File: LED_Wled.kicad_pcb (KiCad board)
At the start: 2 copper layers, 100 x 97.5 mm, 131 parts, among them J1 SWD_PORT_SKEDD, J2 Screw_Terminal_01x02, J3 Screw_Terminal_01x03, Q1 BSS138, U1 ESP8266-12E_ESP-12E, U2 AMS1117-3.3, U3 AMS1117-5.0

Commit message: updated to rev1.1
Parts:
- removed the C1 at (142.0, 128.8)
- removed the C1 at (78.0, 139.2)
- removed the C1 at (142.0, 100.8)
- removed the C1 at (78.0, 111.2)
- removed the C1 at (142.0, 72.8)
- removed the C1 at (78.0, 83.2)
- removed the C2 at (142.0, 123.2)
- removed the C2 at (78.0, 144.8)
- removed the C2 at (142.0, 95.2)
- removed the C2 at (78.0, 116.8)
- removed the C2 at (142.0, 67.2)
- removed the C2 at (78.0, 88.8)
- removed the C3 at (140.0, 131.7)
- removed the C3 at (80.0, 136.3)
- removed the C3 at (140.0, 103.7)
- removed the C3 at (80.0, 108.3)
- removed the C3 at (140.0, 75.7)
- removed the C3 at (80.0, 80.3)
- removed the C4 at (141.3, 134.6)
- removed the C4 at (78.7, 133.4)
- removed the C4 at (141.3, 106.5)
- removed the C4 at (78.7, 105.5)
- removed the C4 at (141.3, 78.5)
- removed the C4 at (78.7, 77.5)
- removed the D1 at (136.3, 134.0)
- removed the D1 at (83.7, 134.0)
- removed the D1 at (136.3, 106.0)
- removed the D1 at (83.7, 106.0)
- removed the D1 at (136.3, 78.0)
- removed the D1 at (83.7, 78.0)
- removed G*** (x6): LOGO, LED_Wled:es
- removed the J1 at (136.2, 143.7)
- removed the J1 at (83.8, 124.3)
- removed the J1 at (136.2, 115.7)
- removed the J1 at (83.8, 96.3)
- removed the J1 at (136.2, 87.7)
- removed the J1 at (83.8, 68.3)
- removed the J2 at (147.0, 144.8)
- removed the J2 at (73.0, 123.2)
- removed the J2 at (147.0, 116.8)
- removed the J2 at (73.0, 95.2)
- removed the J2 at (147.0, 88.8)
- removed the J2 at (73.0, 67.2)
- removed the J3 at (147.0, 137.8)
- removed the J3 at (73.0, 130.2)
- removed the J3 at (147.0, 109.8)
- removed the J3 at (73.0, 102.2)
- removed the J3 at (147.0, 81.8)
- removed the J3 at (73.0, 74.2)
- removed JP1 (x6): Jumper, Jumper:SolderJumper-2_P1.3mm_Open_RoundedPad1.0x1.5mm
- removed the Q1 at (140.0, 138.3)
- removed the Q1 at (80.0, 129.7)
- removed the Q1 at (140.0, 110.3)
- removed the Q1 at (80.0, 101.7)
- removed the Q1 at (140.0, 82.3)
- removed the Q1 at (80.0, 73.7)
- removed the R1 at (132.7, 134.3)
- removed the R1 at (87.3, 133.7)
- removed the R1 at (132.7, 106.3)
- removed the R1 at (87.3, 105.7)
- removed the R1 at (132.7, 78.3)
- removed the R1 at (87.3, 77.7)
- removed the R2 at (132.7, 138.2)
- removed the R2 at (87.3, 129.8)
- removed the R2 at (132.7, 110.2)
- removed the R2 at (87.3, 101.8)
- removed the R2 at (132.7, 82.2)
- removed the R2 at (87.3, 73.8)
- removed the R3 at (132.0, 128.8)
- removed the R3 at (88.0, 139.2)
- removed the R3 at (132.0, 100.8)
- removed the R3 at (88.0, 111.2)
- removed the R3 at (132.0, 72.8)
- removed the R3 at (88.0, 83.2)
- removed the R4 at (136.3, 138.6)
- removed the R4 at (83.7, 129.4)
- removed the R4 at (136.3, 110.6)
- removed the R4 at (83.7, 101.4)
- removed the R4 at (136.3, 82.6)
- removed the R4 at (83.7, 73.4)
- removed the R5 at (139.2, 134.5)
- removed the R5 at (80.8, 133.5)
- removed the R5 at (139.2, 106.5)
- removed the R5 at (80.8, 105.5)
- removed the R5 at (139.2, 78.5)
- removed the R5 at (80.8, 77.5)
- removed the U1 at (120.5, 131.0)
- removed the U1 at (99.5, 137.0)
- removed the U1 at (120.5, 103.0)
- removed the U1 at (99.5, 109.0)
- removed the U1 at (120.5, 75.0)
- removed the U1 at (99.5, 81.0)
- removed the U2 at (136.8, 126.0)
- removed the U2 at (83.2, 142.0)
- removed the U2 at (136.8, 98.0)
- removed the U2 at (83.2, 114.0)
- removed the U2 at (136.8, 70.0)
- removed the U2 at (83.2, 86.0)
- removed the U3 at (147.4, 126.0)
- removed the U3 at (72.6, 142.0)
- removed the U3 at (147.4, 98.0)
- removed the U3 at (72.6, 114.0)
- removed the U3 at (147.4, 70.0)
- removed the U3 at (72.6, 86.0)
- removed mouse-bite-2mm-slot (x17): VAL**, Panelization:mouse-bite-2mm-slot
- added BOOT1: Jumper, Connector_PinHeader_1.27mm:PinHeader_1x02_P1.27mm_Vertical, F.Cu at (112.9, 71.2)
- added C1: 180uF/35V, Capacitor_SMD:CP_Elec_10x12.5, F.Cu at (97.0, 66.8)
- added C2: 470uF/35V, Capacitor_SMD:C_Elec_10x10.2, F.Cu at (84.3, 52.2)
- added C3: 1uF/50V, Capacitor_SMD:C_1206_3216Metric, F.Cu at (93.0, 51.2)
- added C4: 100nF/50V, Capacitor_SMD:C_0805_2012Metric, F.Cu at (110.7, 59.9)
- added C5: 10uF/50V, Capacitor_SMD:C_1206_3216Metric, F.Cu at (112.3, 63.5)
- added D1: SS32, Diode_SMD:D_SMC, F.Cu at (95.3, 57.5)
- added J1: SWD_PORT_SKEDD, LED_Wled:WR_WST_REDFIT_IDC_4Pin, F.Cu at (101.5, 50.0)
- added J2: Screw_Terminal_01x02, TerminalBlock_MetzConnect:TerminalBlock_MetzConnect_Type086_RT03402HBLC_1x02_P3.81mm_Horizontal, F.Cu at (71.8, 53.0)
- added J3: Screw_Terminal_01x03, TerminalBlock_MetzConnect:TerminalBlock_MetzConnect_Type086_RT03403HBLC_1x03_P3.81mm_Horizontal, F.Cu at (71.8, 70.0)
- added L1: 68uH, Inductor_SMD:L_12x12mm_H8mm, F.Cu at (83.0, 65.7)
- added NT1: Net-Tie_2, NetTie:NetTie-2_SMD_Pad2.0mm, F.Cu at (75.5, 57.7)
- added Q1: BSS138, Package_TO_SOT_SMD:SOT-23, F.Cu at (110.7, 50.9)
- added R1: 10k, Resistor_SMD:R_0805_2012Metric, F.Cu at (110.7, 55.8)
- added R2: 10k, Resistor_SMD:R_0805_2012Metric, F.Cu at (110.7, 53.8)
- added R3: 10k, Resistor_SMD:R_0805_2012Metric, F.Cu at (110.7, 57.9)
- added R4: 10k, Resistor_SMD:R_0805_2012Metric, F.Cu at (113.6, 50.9)
- added R5: 10k, Resistor_SMD:R_0805_2012Metric, F.Cu at (110.7, 48.1)
- added U1: ESP8266-12E_ESP-12E, LED_Wled:ESP-12E, F.Cu at (123.5, 62.5)
- added U2: XL1509, Package_SO:SOP-8_3.9x4.9mm_P1.27mm, F.Cu at (104.6, 57.6)
- added U3: LD1117DT33TR, Package_TO_SOT_SMD:TO-252-2, F.Cu at (107.5, 66.8)
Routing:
- net (no net): track 1340.2 -> 0.00 mm, vias 115 -> 0
- net LED_OUT_HV: track 11.2 -> 101.3 mm, vias 0 -> 1
- net VIN: track 25.1 -> 69.9 mm, vias 1 -> 0
- net Net-(D1-Pad1): track 0.00 -> 38.7 mm, vias 0 -> 2
- net Net-(BOOT1-Pad2): track 0.00 -> 30.8 mm
- net +5V: track 18.1 -> 47.0 mm
- net Net-(JP1-Pad2): track 21.1 -> 0.00 mm, vias 2 -> 0
- net /PROT_VIN: track 18.5 -> 0.00 mm
- net GNDPWR: track 0.00 -> 10.8 mm
- net TXD: track 26.8 -> 35.6 mm, vias 0 -> 1
- net Net-(R3-Pad1): track 20.3 -> 28.3 mm
- net RXD: track 25.9 -> 31.4 mm, vias 0 -> 1
- net Net-(R1-Pad2): track 3.91 -> 7.27 mm
- net LED_OUT_LV: track 39.8 -> 37.7 mm, vias 3 -> 0
- net GND: track 9.71 -> 7.65 mm, vias 13 -> 57
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- removed copper zone on B.Cu, net (none)
- removed copper zone on F.Cu, net (none)
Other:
- board size 100 x 97.5 mm -> 66 x 27 mm
- board text added: "For use with ARGB LED-strip MAX INPUT: +30 V"
- board text added: "remote-led-project 2022-01-13 rev1.1"
- board text removed: "+3v3"
- board text removed: "DI VIN GND"
- board text removed: "For use with ARGB LED-strip MAX INPUT: +13V"
- board text removed: "GND"
- board text removed: "RX"
- board text removed: "TX"
- board text removed: "VIN GND"
- board text removed: "remote-led-project 2021-11-04 rev1.0"

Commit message: Update LED_Wled.kicad_pcb
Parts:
- added G***: LOGO, LED_Wled:es, B.Cu at (122.2, 60.0)

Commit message: finished rev1.1
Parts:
- removed G***: LOGO, LED_Wled:es
- added F1: Fuse_Small, Fuse:Fuse_1812_4532Metric, F.Cu at (93.3, 50.6)
- C1: value 180uF/35V -> 180uF/63V; footprint Capacitor_SMD:CP_Elec_10x12.5 -> Capacitor_THT:C_Radial_D10.0mm_H16.0mm_P5.00mm
- J2: value Screw_Terminal_01x02 -> KF141V-2.54-2P; footprint TerminalBlock_MetzConnect:TerminalBlock_MetzConnect_Type086_RT03402HBLC_1x02_P3.81mm_Horizontal -> userdvc:KF141V-2.54-2P
- J3: value Screw_Terminal_01x03 -> KF141V-2.54-3P; footprint TerminalBlock_MetzConnect:TerminalBlock_MetzConnect_Type086_RT03403HBLC_1x03_P3.81mm_Horizontal -> userdvc:KF141V-2.54-3P
- moved C3 10.0 mm to (85.9, 58.3), turned to 180 degrees
- moved J3 4.39 mm to (70.0, 66.0), turned to 270 degrees
- moved C1 3.76 mm to (100.8, 66.5)
- moved J2 2.34 mm to (70.0, 51.5), turned to 270 degrees
- moved L1 0.78 mm to (83.5, 66.3)
- moved NT1 0.74 mm to (76.0, 58.2)
- moved C2 0.71 mm to (84.2, 51.5)
- moved J1 0.50 mm to (102.0, 50.0)
- moved D1 0.20 mm to (95.5, 57.5)
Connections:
- C2 pad 1: VIN -> Net-(C2-Pad1)
- C3 pad 1: VIN -> Net-(C2-Pad1)
- U2 pad 1: VIN -> Net-(C2-Pad1)
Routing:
- net VIN: track 69.9 -> 26.8 mm
- net Net-(C2-Pad1): track 0.00 -> 33.3 mm
- net LED_OUT_LV: track 37.7 -> 31.4 mm, vias 0 -> 2
- net LED_OUT_HV: track 101.3 -> 107.1 mm
- net GNDPWR: track 10.8 -> 16.3 mm
- net GND: track 7.65 -> 11.3 mm, vias 57 -> 70
- net Net-(D1-Pad1): track 38.7 -> 40.2 mm
- net TXD: track 35.6 -> 36.2 mm
- added copper zone on F.Cu, net GNDPWR
- added copper zone on B.Cu, net VIN
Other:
- board size 66 x 27 mm -> 67 x 27 mm
- board text added: "D_OUT"
- board text added: "GNDPWR"
- board text added: "VIN"

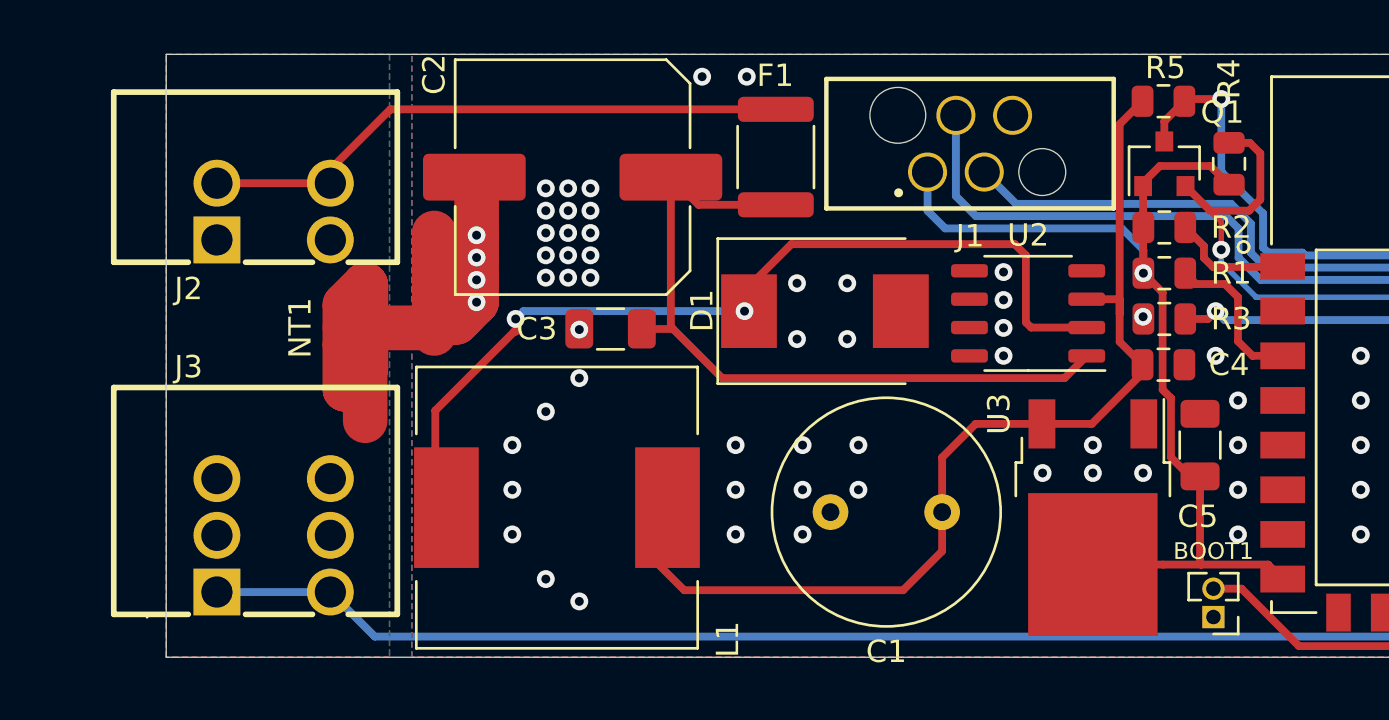
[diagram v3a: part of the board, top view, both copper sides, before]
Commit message: revised pcb, fixed library issues, changed 3.3v component to basic component, added docs and readme
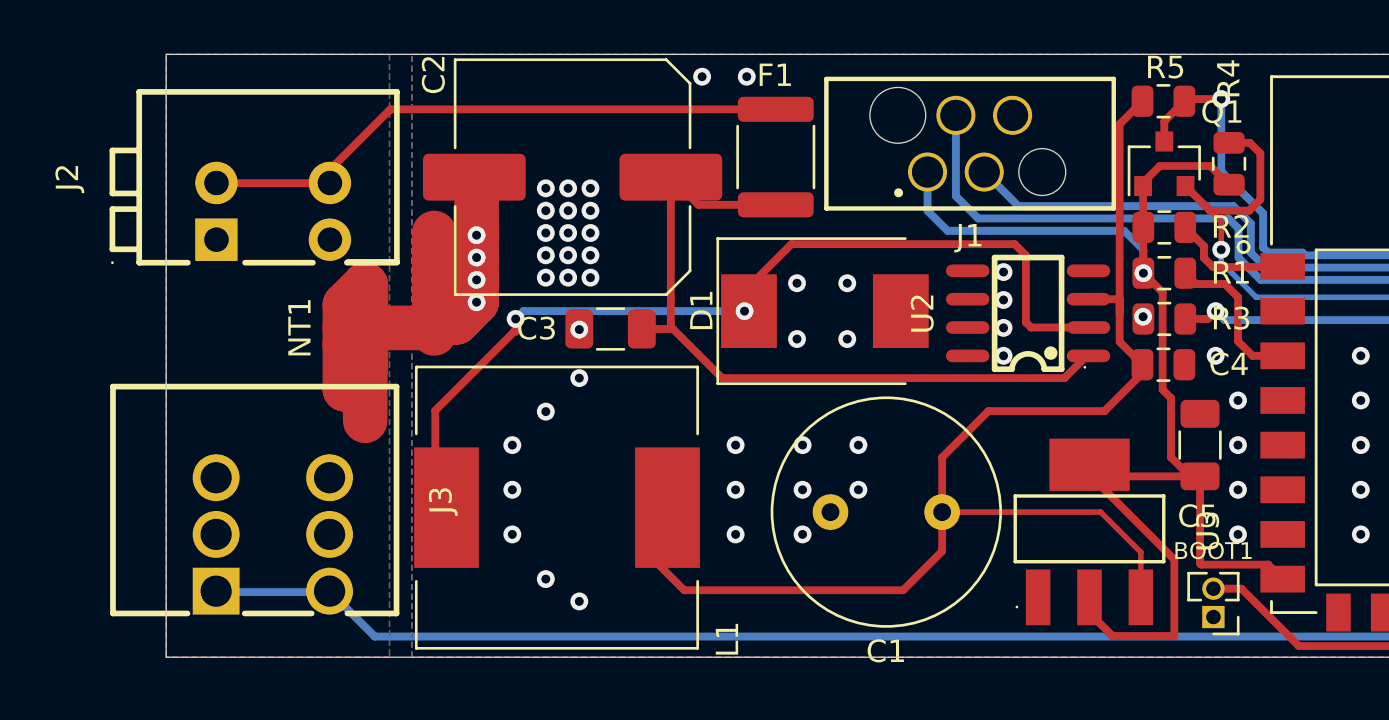
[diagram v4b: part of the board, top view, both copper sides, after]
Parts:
- J2: footprint userdvc:KF141V-2.54-2P -> LED_Wled:CONN-TH_2P-P2.54_KF141V-2.54-2P
- J3: footprint userdvc:KF141V-2.54-3P -> LED_Wled:CONN-TH_3P-P2.54_KF141V-2.54-3P
- U2: footprint Package_SO:SOP-8_3.9x4.9mm_P1.27mm -> LED_Wled:SOIC-8_L5.0-W4.0-P1.27-LS6.0-BL
- U3: value LD1117DT33TR -> AMS1117-3.3; footprint Package_TO_SOT_SMD:TO-252-2 -> LED_Wled:SOT-223-3_L6.5-W3.4-P2.30-LS7.0-BR
- moved J2 1.72 mm to (70.8, 53.0), turned to 90 degrees
- moved J3 1.69 mm to (70.8, 67.5)
- moved U3 0.62 mm to (107.3, 67.3)
- turned U2 to 90 degrees
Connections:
- U1 pad 10: (no net) -> unconnected-(U1-MISO-Pad10)
- U1 pad 11: (no net) -> unconnected-(U1-IO9-Pad11)
- U1 pad 12: (no net) -> unconnected-(U1-IO10-Pad12)
- U1 pad 13: (no net) -> unconnected-(U1-MOSI-Pad13)
- U1 pad 14: (no net) -> unconnected-(U1-SCLK-Pad14)
- U1 pad 17: (no net) -> unconnected-(U1-IO2-Pad17)
- U1 pad 2: (no net) -> unconnected-(U1-ADC-Pad2)
- U1 pad 20: (no net) -> unconnected-(U1-IO5-Pad20)
- U1 pad 4: (no net) -> unconnected-(U1-IO16-Pad4)
- U1 pad 5: (no net) -> unconnected-(U1-IO14-Pad5)
- U1 pad 6: (no net) -> unconnected-(U1-IO12-Pad6)
- U1 pad 7: (no net) -> unconnected-(U1-IO13-Pad7)
- U1 pad 9: (no net) -> unconnected-(U1-CS0-Pad9)
- U2 pad 4: (no net) -> unconnected-(U2-ON/OFF-Pad4)
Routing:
- net +3V3: track 44.9 -> 59.4 mm
- net +5V: track 47.0 -> 58.6 mm
- net GND: vias 70 -> 66
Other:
- net class Default removed

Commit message: new release, v1.2, prod files ready
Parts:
- removed F1: Fuse_Small, Fuse:Fuse_1812_4532Metric
- removed NT1: Net-Tie_2, NetTie:NetTie-2_SMD_Pad2.0mm
- added J4: Conn_01x01, TestPoint:TestPoint_Pad_4.0x4.0mm, F.Cu at (73.4, 52.8)
- added JP1: SolderJumper_3_Open, LED_Wled:BIG JUMPER, F.Cu at (73.5, 65.7)
- added SYM1: LOGO, LED_Wled:easyled, B.Cu at (94.6, 59.5)
- C1: value 180uF/63V -> 220uF/35V; footprint Capacitor_THT:C_Radial_D10.0mm_H16.0mm_P5.00mm -> Capacitor_SMD:C_Elec_8x10.2
- D1: value SS32 -> SS54; footprint Diode_SMD:D_SMC -> Diode_SMD:D_SMA
- J2: value KF141V-2.54-2P -> Conn_01x01; footprint LED_Wled:CONN-TH_2P-P2.54_KF141V-2.54-2P -> TestPoint:TestPoint_Pad_4.0x4.0mm
- J3: value KF141V-2.54-3P -> Conn_01x01; footprint LED_Wled:CONN-TH_3P-P2.54_KF141V-2.54-3P -> TestPoint:TestPoint_Pad_2.0x2.0mm
- L1: footprint Inductor_SMD:L_12x12mm_H8mm -> LED_Wled:IND-SMD_L12.5-W12.5
- Q1: value BSS138 -> 2N7002
- moved J3 19.4 mm to (73.5, 48.3)
- moved J2 5.57 mm to (73.4, 58.0), turned to -90 degrees
- moved C1 3.35 mm to (97.4, 66.4)
- moved C3 2.35 mm to (88.2, 58.3), turned to 0 degrees
- moved J1 2.33 mm to (99.7, 50.0)
- moved U2 0.85 mm to (103.8, 57.6)
- moved D1 0.75 mm to (94.8, 57.5)
- turned L1 to 180 degrees
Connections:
- C2 pad 1: Net-(U2-VIN) -> VIN
- C3 pad 1: Net-(U2-VIN) -> VIN
- J2 pad 1: GNDPWR -> VIN
- U2 pad 1: Net-(U2-VIN) -> VIN
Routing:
- net Net-(U2-VIN): track 33.3 -> 0.00 mm
- net +5V: track 58.6 -> 91.3 mm
- net LED_OUT_HV: track 107.1 -> 129.9 mm, vias 1 -> 2
- net VIN: track 26.8 -> 44.1 mm
- net GNDPWR: track 16.3 -> 0.00 mm
- net RXD: track 31.7 -> 34.7 mm
- net Net-(D1-K): track 40.2 -> 42.8 mm
- net TXD: track 36.2 -> 38.8 mm
- net +3V3: track 59.4 -> 61.6 mm
- net GND: track 11.3 -> 9.74 mm, vias 66 -> 71
- added copper zone on F.Cu, net VIN
- removed copper zone on F.Cu, net GNDPWR
- removed copper zone on B.Cu, net VIN
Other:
- board size 67 x 27 mm -> 63 x 27 mm
- board text added: "DATA"
- board text added: "For use with ARGB LED-strip MAX INPUT: +24 V !SELECT INPUT BY SOLDER!"
- board text added: "GND"
- board text added: "VIN LED_O +5V"
- board text added: "wEasyLed_V1 2025-01-28 rev1.2"
- board text removed: "D_OUT"
- board text removed: "For use with ARGB LED-strip MAX INPUT: +30 V"
- board text removed: "GNDPWR"
- board text removed: "remote-led-project 2022-01-13 rev1.1"
